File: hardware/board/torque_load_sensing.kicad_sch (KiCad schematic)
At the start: 25 parts, among them J3 Conn_01x05_Female, U16 AD8615, U7 AD8226, U8 ADS7049

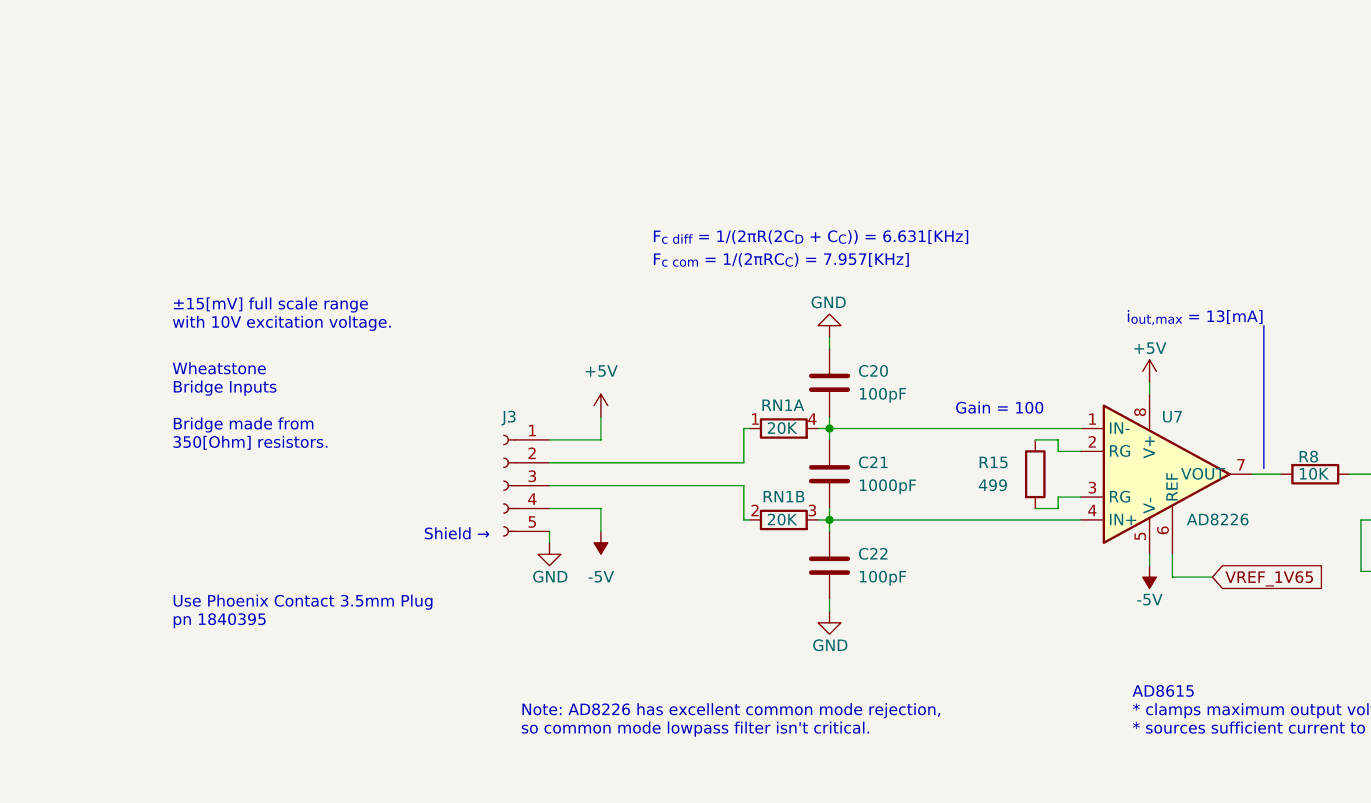
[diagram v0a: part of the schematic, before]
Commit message: add tvs diodes to inputs
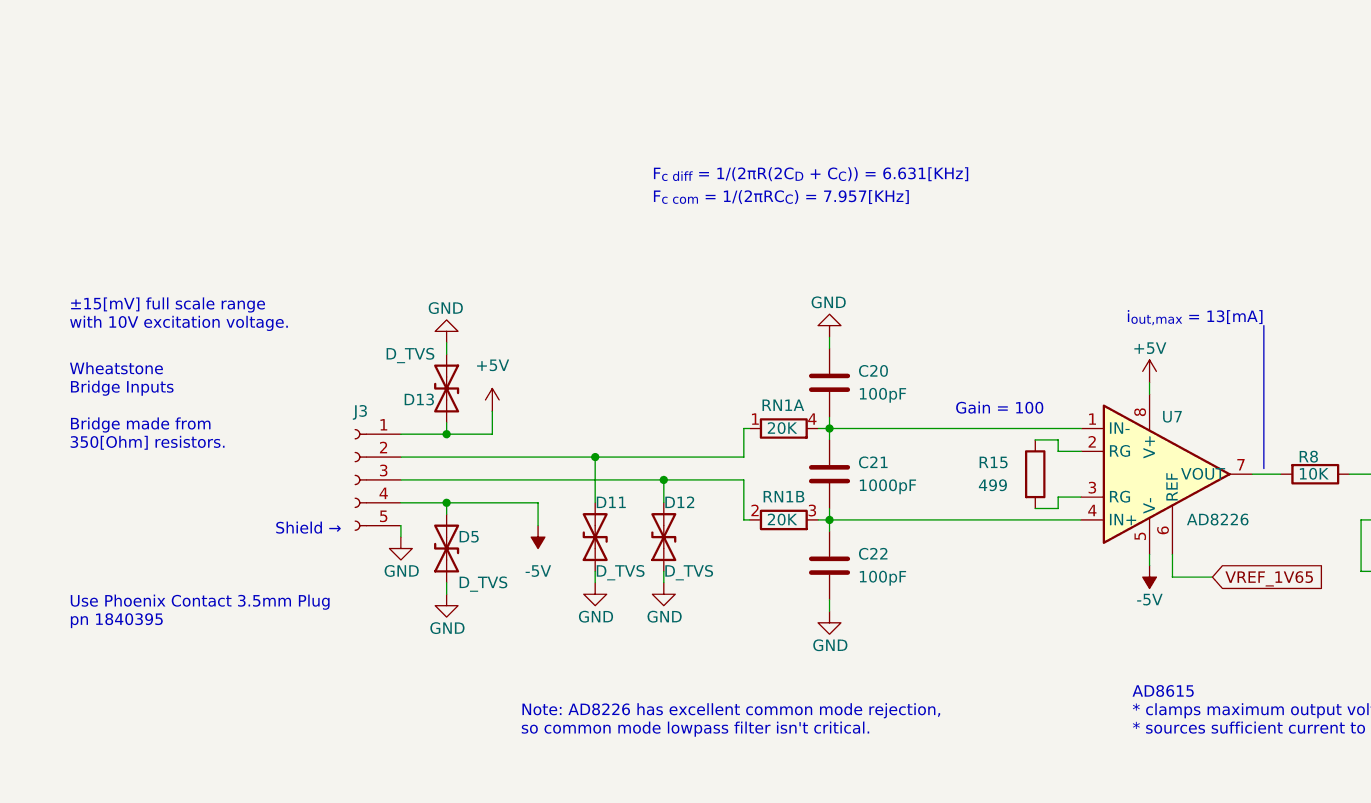
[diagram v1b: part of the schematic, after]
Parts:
- added D11, D12, D13, D5: D_TVS, Diode_SMD:D_SOD-882D, symbol Device:D_TVS
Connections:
- net +5V: now also D13.2 (A2)
- net -5V: now also D5.2 (A2)
- net GND: now also D11.1 (A1), D12.1 (A1), D13.1 (A1), D5.1 (A1)
- net at J3.3 (Pin_3), RN1.2 (R2.1): now also D12.2 (A2)
- net at J3.2 (Pin_2), RN1.1 (R1.1): now also D11.2 (A2)
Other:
- moved on the sheet: J3
